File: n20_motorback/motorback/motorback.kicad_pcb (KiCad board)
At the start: 2 copper layers, 12 x 16 mm, 10 parts, among them J1 Conn_01x03_Male, J2 Conn_01x01_Male, J3 Conn_01x01_Male, U1 DRV8837, U2 ATtiny13V-10SSU

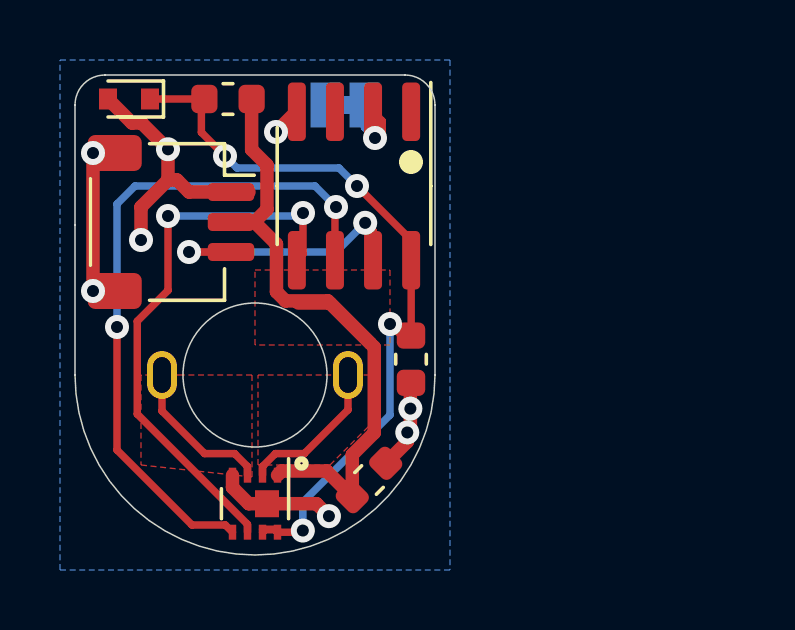
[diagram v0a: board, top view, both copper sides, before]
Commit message: update to linear regulator
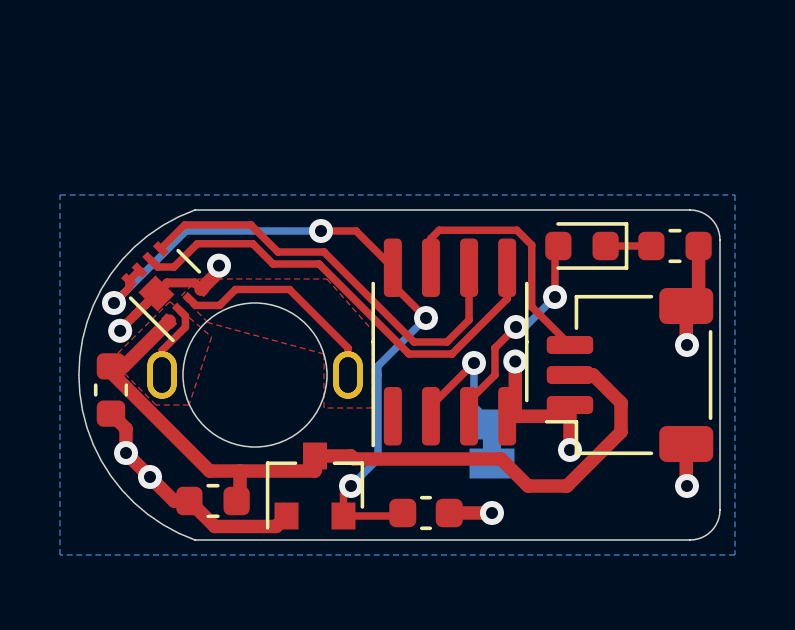
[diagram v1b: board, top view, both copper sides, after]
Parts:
- added C3: 1uF, Capacitor_SMD:C_0603_1608Metric, F.Cu at (165.7, 124.6)
- added U3: generic_regulator_GOI, Package_TO_SOT_SMD:SOT-23, F.Cu at (162.0, 123.7)
- C2: value 0.1uf -> 1uF
- D1: value MM5Z5V1 -> LED; footprint Diode_SMD:D_SOD-523 -> LED_SMD:LED_0603_1608Metric
- J1: value Conn_01x03_Male -> Servo wire input
- R1: value 330R -> 2.2k
- U1: value DRV8837 -> DRV8837DSGR
- moved J1 16.1 mm to (172.5, 120.0), turned to 90 degrees
- moved D1 15.9 mm to (170.9, 115.7)
- moved R1 15.7 mm to (174.0, 115.7)
- moved JP1 12.3 mm to (167.9, 122.3), turned to 90 degrees
- moved C1 9.11 mm to (155.2, 120.5), turned to -90 degrees
- moved C2 8.12 mm to (158.6, 124.2), turned to 180 degrees
- moved U1 7.88 mm to (157.0, 117.0), turned to 135 degrees
- moved J2 6.20 mm to (156.8, 120.0)
- moved J3 6.20 mm to (163.1, 120.0)
- moved U2 6.11 mm to (166.5, 118.9), turned to 90 degrees
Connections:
- net Net-(J2-Pad1) renamed /MOTOROUT1
- net Net-(J3-Pad1) renamed /MOTOROUT2
- net Net-(U2-Pad1) renamed no_connect_12
- C2 pad 1: /VLOGIC -> VBAT
- D1 pad 1: /VLOGIC -> Net-(D1-Pad1)
- D1 pad 2: GND -> BLINKY
- R1 pad 1: VBAT -> GND
- R1 pad 2: /VLOGIC -> Net-(D1-Pad1)
- U2 pad 3: Net-(U2-Pad3) -> BLINKY
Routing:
- net /MOTORR: track 22.8 -> 14.3 mm, vias 2 -> 0
- net BLINKY: track 0.00 -> 7.08 mm, vias 0 -> 2
- net VBAT: track 23.1 -> 26.9 mm
- net GND: track 21.8 -> 25.5 mm, vias 8 -> 9
- net /MOTORF: track 18.7 -> 15.6 mm, vias 2 -> 0
- net /MOTOROUT1: track 5.08 -> 2.55 mm
- net /CONFIG1: track 2.35 -> 4.67 mm
- net /MOTOROUT2: track 5.11 -> 7.26 mm
- net Net-(D1-Pad1): track 0.00 -> 1.53 mm
- net /VLOGIC: track 25.0 -> 24.1 mm
- net PWMIN: track 9.03 -> 8.51 mm, vias 2 -> 0
- removed copper zone on F.Cu, net VBAT
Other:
- board size 12 x 16 mm -> 21.4 x 11 mm
- board text removed: "Right"

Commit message: misc update
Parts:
- R1: value 2.2k -> 1k
- U3: value generic_regulator_GOI -> AIC1734-33GUTR
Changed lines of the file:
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@@
     (descr "Resistor SMD 0603 (1608 Metric), square (rectangular) end terminal, IPC_7351 nominal, (Body size source: http://www.tortai-tech.com/upload/download/2011102023233369053.pdf), generated with kicad-footprint-generator")
     (tags "resistor")
-    (property "LCSC" "")
+    (property "LCSC" "C21190")
     (property "Sheet file" "motorback.kicad_sch")
     (property "Sheet name" "")
@@
       (effects (font (size 1 1) (thickness 0.15)))
     )
-    (fp_text value "2.2k" (at 0 1.43) (layer "F.Fab")
+    (fp_text value "1k" (at 0 1.43) (layer "F.Fab")
       (effects (font (size 1 1) (thickness 0.15)))
     )
@@
     (descr "Capacitor SMD 0603 (1608 Metric), square (rectangular) end terminal, IPC_7351 nominal, (Body size source: http://www.tortai-tech.com/upload/download/2011102023233369053.pdf), generated with kicad-footprint-generator")
     (tags "capacitor")
-    (property "LCSC" "")
+    (property "LCSC" "C15849")
     (property "Sheet file" "motorback.kicad_sch")
     (property "Sheet name" "")
@@
     (descr "SOT-23, Standard")
     (tags "SOT-23")
+    (property "LCSC" "C211659")
     (property "Sheet file" "motorback.kicad_sch")
     (property "Sheet name" "")
@@
       (effects (font (size 1 1) (thickness 0.15)))
     )
-    (fp_text value "generic_regulator_GOI" (at 0 2.5 90) (layer "F.Fab")
+    (fp_text value "AIC1734-33GUTR" (at 0 2.5 90) (layer "F.Fab")
       (effects (font (size 1 1) (thickness 0.15)))
     )
@@
     (descr "Capacitor SMD 0603 (1608 Metric), square (rectangular) end terminal, IPC_7351 nominal, (Body size source: IPC-SM-782 page 76, https://www.pcb-3d.com/wordpress/wp-content/uploads/ipc-sm-782a_amendment_1_and_2.pdf), generated with kicad-footprint-generator")
     (tags "capacitor")
-    (property "LCSC" "")
+    (property "LCSC" "C15849")
     (property "Sheet file" "motorback.kicad_sch")
     (property "Sheet name" "")
@@
     (descr "SOIC, 8 Pin (JEDEC MS-012AA, https://www.analog.com/media/en/package-pcb-resources/package/pkg_pdf/soic_narrow-r/r_8.pdf), generated with kicad-footprint-generator ipc_gullwing_generator.py")
     (tags "SOIC SO")
-    (property "LCSC" "C40382")
+    (property "LCSC" "C14075")
     (property "Sheet file" "motorback.kicad_sch")
     (property "Sheet name" "")
@@
     (descr "LED SMD 0603 (1608 Metric), square (rectangular) end terminal, IPC_7351 nominal, (Body size source: http://www.tortai-tech.com/upload/download/2011102023233369053.pdf), generated with kicad-footprint-generator")
     (tags "LED")
+    (property "LCSC" "C2286")
     (property "Sheet file" "motorback.kicad_sch")
     (property "Sheet name" "")
@@
       (net 11 "/CONFIG1") (pinfunction "2"))
   )
+  (gr_circle (center 163 121.8) (end 163.4 121.8) (layer "F.SilkS") (width 0.12) (fill solid))
+  (gr_circle (center 156.2 118.9) (end 156.6 118.9) (layer "F.SilkS") (width 0.12) (fill solid))
   (gr_circle (center 160 120) (end 166 120) (layer "Dwgs.User") (width 0.1) (fill none))
   (gr_circle (center 156.9 120) (end 157.1 120) (layer "Dwgs.User") (width 0.1) (fill none))

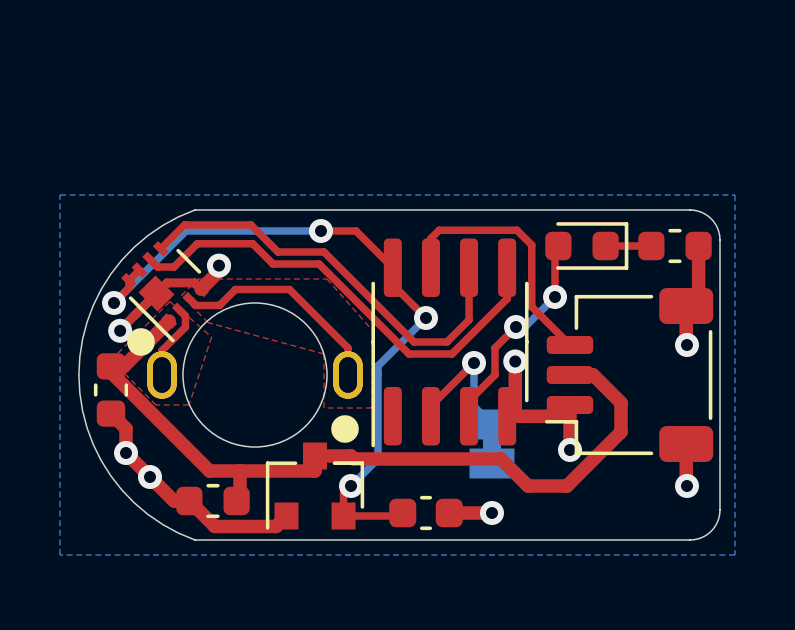
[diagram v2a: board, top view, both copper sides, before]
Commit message: dimension fixes
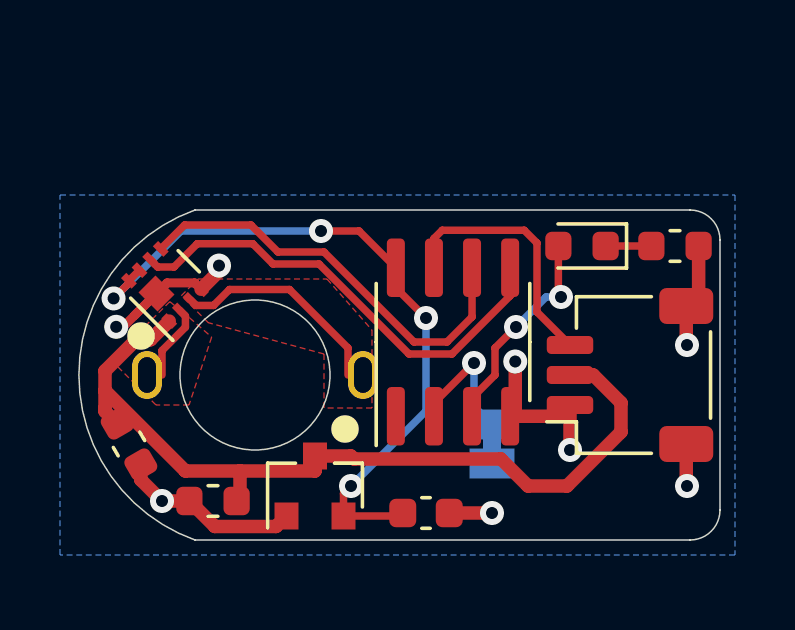
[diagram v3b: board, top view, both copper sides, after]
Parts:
- moved C1 1.90 mm to (155.8, 122.3), turned to -60 degrees
- moved J2 0.50 mm to (156.3, 120.0)
- moved J3 0.50 mm to (163.6, 120.0)
- moved U2 0.10 mm to (166.6, 118.9)
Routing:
- net GND: track 25.5 -> 23.6 mm, vias 9 -> 8
- net VBAT: track 26.9 -> 28.8 mm
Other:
- outline, holes or cut-outs redrawn

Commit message: dimension fixes and move cap
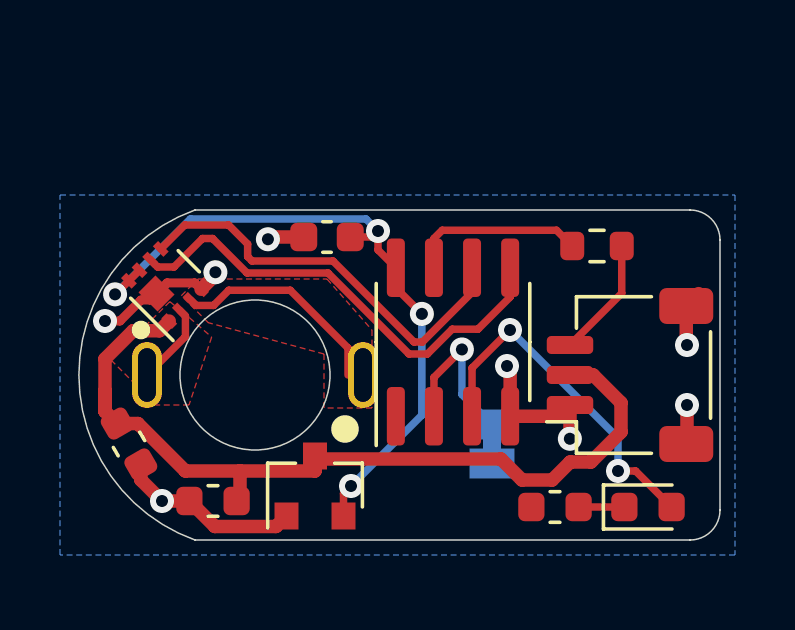
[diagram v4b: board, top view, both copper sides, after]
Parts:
- added R2: 680R, Resistor_SMD:R_0603_1608Metric, F.Cu at (171.4, 115.7)
- R1: value 1k -> 680R
- moved C3 9.77 mm to (162.4, 115.4), turned to 180 degrees
- moved R1 9.58 mm to (170.0, 124.4), turned to 0 degrees
- moved D1 8.97 mm to (173.1, 124.4), turned to 0 degrees
- moved J2 0.10 mm to (156.4, 120.0)
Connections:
- net no_connect_12 renamed no_connect_13
- U2 pad 7: PWMIN -> /PWMR
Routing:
- net /PWMR: track 0.00 -> 5.92 mm
- net BLINKY: track 7.23 -> 11.9 mm
- net PWMIN: track 8.56 -> 4.01 mm
- net GND: track 23.6 -> 20.2 mm
- net /CONFIG1: track 4.63 -> 5.53 mm
- net /VLOGIC: track 24.0 -> 23.3 mm
